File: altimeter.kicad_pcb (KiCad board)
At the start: 2 copper layers, 45 x 24 mm, 50 parts, among them J201 Conn_01x10, J202 Conn_ARM_JTAG_SWD_10, J203 Conn_02x03_Counter_Clockwise, J204 Conn_01x04, J205 USB_B_Micro, Q101 DMG2301L, Q302 BC847BDW1, Q402 BC847BDW1, Q502 BC847BDW1, U101 STM32F302CCTx, U102 MS5611-01BA, U103 MIC5219-3.3YM5, U104 LF50_TO252, U105 LM397, U106 MT25Q, U107 AIS2120SXTR, U301 SI7232DN, U501 SI7232DN, Y101 Crystal_Small

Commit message: more work on schematic and layout
Signed-off-by: Thomas Schmid <tom@lfence.de>
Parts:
- removed the R302 at (141.7, 98.0)
- removed R305, R405, R505: R, Resistor_SMD:R_0402_1005Metric
- removed the R402 at (128.3, 103.4)
- removed the R502 at (151.2, 130.5)
- added F301: Polyfuse, Fuse:Fuse_0603_1608Metric_Pad1.05x0.95mm_HandSolder, F.Cu at (142.0, 105.0)
- added F401: Polyfuse, Fuse:Fuse_0603_1608Metric_Pad1.05x0.95mm_HandSolder, F.Cu at (140.0, 115.5)
- added F501: Polyfuse, Fuse:Fuse_0603_1608Metric_Pad1.05x0.95mm_HandSolder, F.Cu at (140.5, 107.0)
- C101, C102: value C_Small -> 22p
- C104: renamed from C103; value C_Small -> 100n
- C107: renamed from C105; value C_Small -> 2.2u
- J203: footprint Connector_PinHeader_2.00mm:PinHeader_2x05_P2.00mm_Vertical_SMD -> Connector_PinHeader_2.54mm:PinHeader_2x03_P2.54mm_Horizontal
- R101, R102: value R -> 680
- R301, R401, R501: value R -> 2.7k
- R302: renamed from R303; value R -> 33
- R303: renamed from R304; value R -> 2.7k
- R402: renamed from R403; value R -> 33
- R403: renamed from R404; value R -> 2.7k
- R502: renamed from R503; value R -> 33
- R503: renamed from R504; value R -> 2.7k
- U101: moved to B.Cu
- U103: renamed from U107; moved to B.Cu
- U106: renamed from U105; moved to B.Cu
- U107: renamed from U102; moved to B.Cu
- moved D102 46.4 mm to (166.0, 99.0), turned to 90 degrees
- moved D101 45.1 mm to (164.5, 99.0), turned to 90 degrees
- moved J202 16.0 mm to (155.0, 117.0)
- moved U107 13.0 mm to (159.5, 106.5), turned to 90 degrees
- moved Q101 12.6 mm to (167.0, 106.0)
- moved U106 11.9 mm to (165.5, 104.0)
- moved Q401 11.7 mm to (140.5, 112.0)
- moved Y101 8.35 mm to (154.5, 124.5), turned to 180 degrees
- moved U102 6.36 mm to (169.0, 115.0)
- moved U103 5.93 mm to (172.5, 106.0), turned to 180 degrees
- moved U501 3.94 mm to (143.5, 115.5)
- moved U101 1.30 mm to (158.0, 115.5)
- turned U105 to 180 degrees
- renumbered C104 to C105, C107 to C106, C106 to C108, J205 to J204, J204 to J205, Q302 to Q301, Q402 to Q401, Q502 to Q501, U106 to U102, U103 to U104, U104 to U105

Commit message: update
Signed-off-by: Thomas Schmid <tom@lfence.de>
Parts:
- removed U106: LM397, Package_TO_SOT_SMD:SOT-23-5_HandSoldering
- removed Y101: Crystal_Small, Crystal:Crystal_SMD_5032-2Pin_5.0x3.2mm_HandSoldering
- added C103: 1u, Capacitor_SMD:C_0603_1608Metric_Pad1.05x0.95mm_HandSolder, B.Cu at (164.5, 107.4)
- added C3: CP, Capacitor_THT:CP_Axial_L11.0mm_D8.0mm_P15.00mm_Horizontal, F.Cu at (150.0, 100.4)
- added Y1: Crystal_GND24, Crystal:Crystal_SMD_2520-4Pin_2.5x2.0mm, B.Cu at (151.8, 118.2)
- C101, C102: footprint Capacitor_SMD:C_0603_1608Metric_Pad1.05x0.95mm_HandSolder -> Capacitor_SMD:C_0402_1005Metric; moved to B.Cu
- C104: footprint Capacitor_SMD:C_0603_1608Metric_Pad1.05x0.95mm_HandSolder -> Capacitor_SMD:C_0805_2012Metric_Pad1.15x1.40mm_HandSolder; moved to B.Cu
- C107, F301, F401, F501, Q101, Q301, Q401, Q501, R301, R302, R303, R401, R402, R403, R501, R502, R503, U301, U501: moved to B.Cu
- H201, H202: footprint MountingHole:MountingHole_3.2mm_M3_DIN965 -> MountingHole:MountingHole_3.2mm_M3_Pad_Via
- moved C107 47.8 mm to (153.2, 99.8)
- moved C104 44.1 mm to (153.4, 101.3)
- moved C106 41.5 mm to (157.4, 112.1)
- moved R102 39.3 mm to (168.0, 102.4), turned to 90 degrees
- moved R101 37.1 mm to (166.6, 102.4), turned to 90 degrees
- moved C101 37.1 mm to (154.0, 118.2), turned to 90 degrees
- moved R104 33.6 mm to (176.8, 104.0)
- moved R103 33.3 mm to (174.5, 104.3)
- moved C105 32.5 mm to (167.3, 108.1)
- moved Q501 29.9 mm to (141.4, 105.1)
- moved C108 29.8 mm to (172.8, 107.2)
- moved R503 29.5 mm to (139.0, 106.1)
- moved R502 28.5 mm to (139.4, 104.5), turned to 90 degrees
- moved R201 27.7 mm to (173.0, 102.9)
- moved C102 27.5 mm to (149.4, 118.2), turned to 270 degrees
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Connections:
- U301 pad 1: FIRE_PYRO1 -> FIRE_PYRO2
- U301 pad 3: FIRE_PYRO2 -> FIRE_PYRO1
- U301 pad 5: PYRO2_LOW -> PYRO1_LOW
- U301 pad 6: PYRO1_LOW -> PYRO2_LOW
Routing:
- net PYRO_TEST_ENABLE: track 0.00 -> 6.40 mm
- net Net-(Q501-Pad1): track 0.00 -> 4.28 mm
- net Net-(Q401-Pad1): track 0.00 -> 4.28 mm
- net GND: track 0.00 -> 4.22 mm
- net Net-(Q501-Pad2): track 0.00 -> 1.94 mm
- net Net-(Q401-Pad2): track 0.00 -> 1.94 mm
- net Net-(F501-Pad2): track 0.00 -> 1.48 mm
- net Net-(F401-Pad2): track 0.00 -> 1.48 mm
- net Net-(Q301-Pad2): track 3.29 -> 1.94 mm
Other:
- net class Default: clearance 0.2 -> 0.1651; trace_width 0.25 -> 0.1778
- rule trace_clearance: 0.2 -> 0.1651
- rule trace_min: 0.2 -> 0.1524

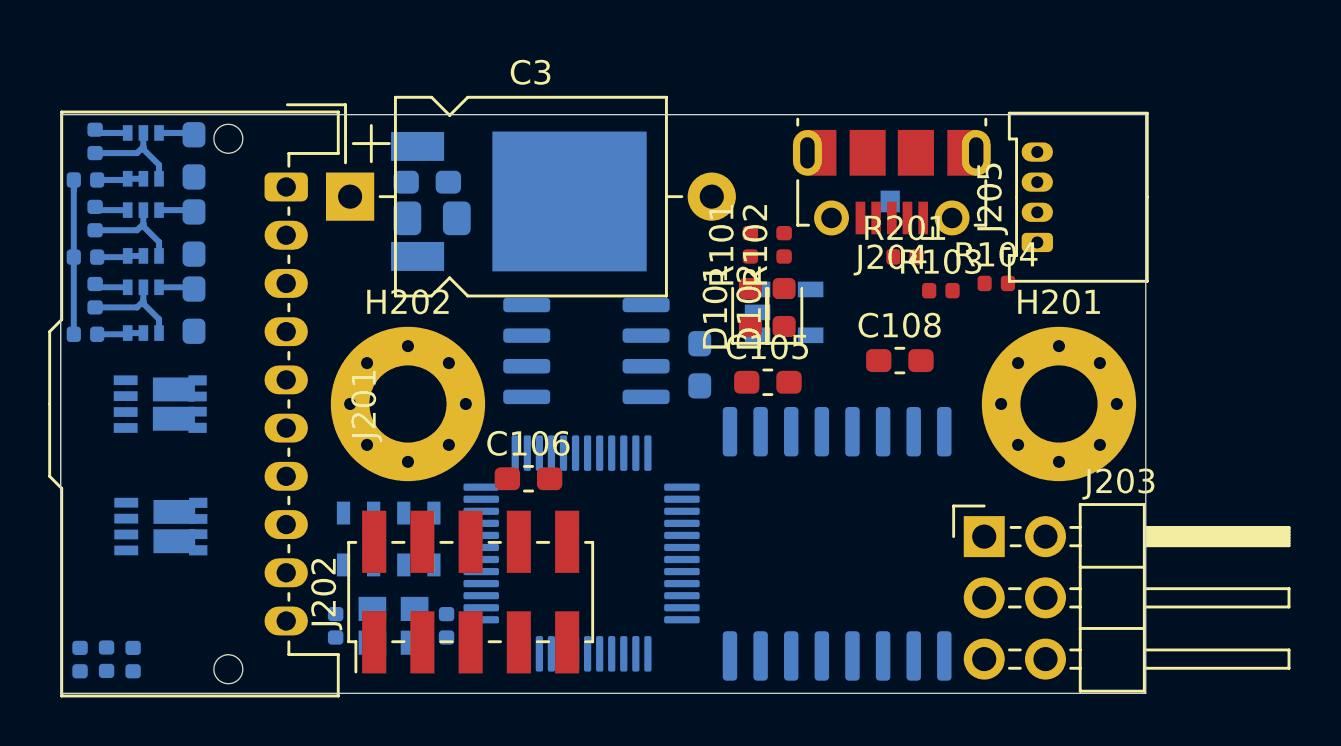
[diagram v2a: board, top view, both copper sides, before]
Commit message: update to schematic and layout
Signed-off-by: Thomas Schmid <tom@lfence.de>
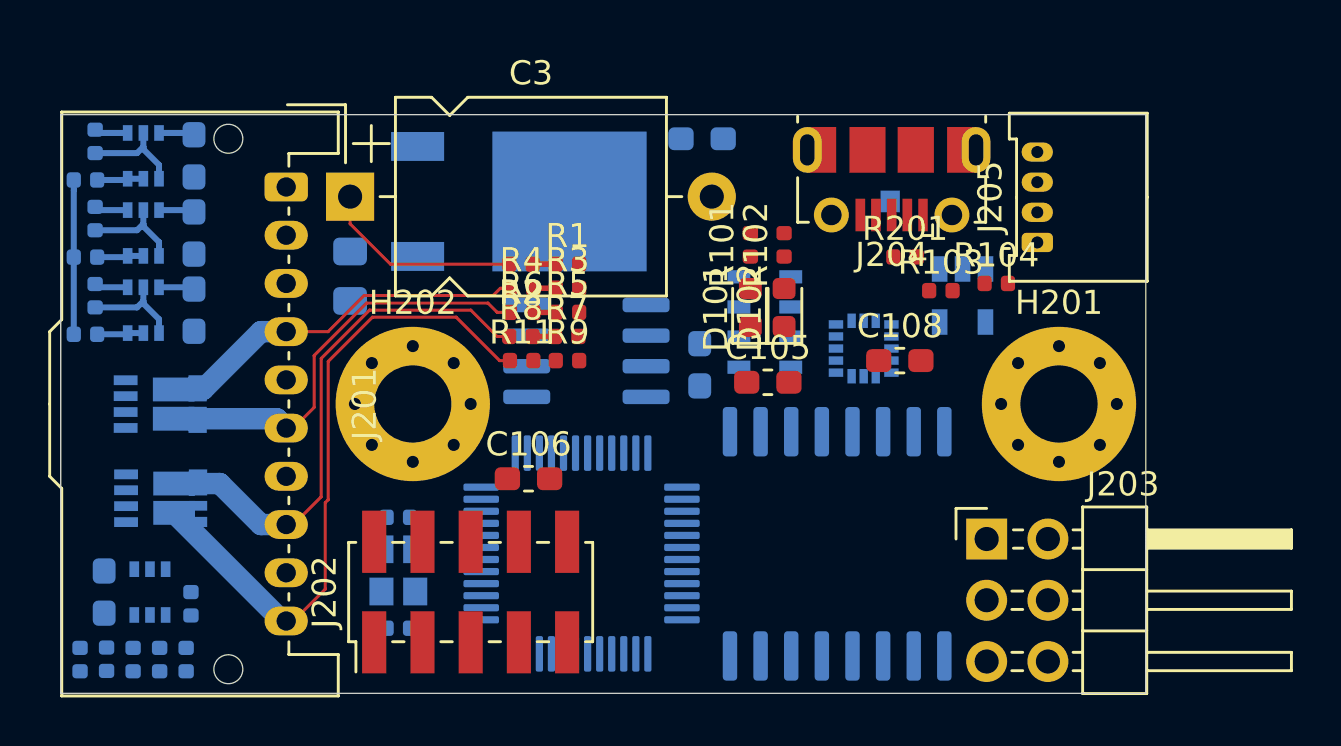
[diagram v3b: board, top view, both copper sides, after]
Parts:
- added F1: Polyfuse, Fuse:Fuse_0603_1608Metric_Pad1.05x0.95mm_HandSolder, B.Cu at (139.8, 116.8)
- added Q1: BC847BDW1, Package_TO_SOT_SMD:SOT-363_SC-70-6, B.Cu at (141.7, 116.8)
- added R1: 68k, Resistor_SMD:R_0402_1005Metric, F.Cu at (159.0, 103.2)
- added R10: 2.7k, Resistor_SMD:R_0402_1005Metric, B.Cu at (142.1, 119.6)
- added R11: 220k, Resistor_SMD:R_0402_1005Metric, F.Cu at (157.1, 107.2)
- added R12: 33, Resistor_SMD:R_0402_1005Metric, B.Cu at (143.4, 117.3)
- added R13: 2.7k, Resistor_SMD:R_0402_1005Metric, B.Cu at (143.2, 119.6)
- added R2: 220k, Resistor_SMD:R_0402_1005Metric, F.Cu at (157.1, 103.2)
- added R3: 68k, Resistor_SMD:R_0402_1005Metric, F.Cu at (159.0, 104.2)
- added R4: 220k, Resistor_SMD:R_0402_1005Metric, F.Cu at (157.1, 104.2)
- added R5: 68k, Resistor_SMD:R_0402_1005Metric, F.Cu at (159.0, 105.2)
- added R6: 220k, Resistor_SMD:R_0402_1005Metric, F.Cu at (157.1, 105.2)
- added R7: 68k, Resistor_SMD:R_0402_1005Metric, F.Cu at (159.0, 106.2)
- added R8: 220k, Resistor_SMD:R_0402_1005Metric, F.Cu at (157.1, 106.2)
- added R9: 68k, Resistor_SMD:R_0402_1005Metric, F.Cu at (159.0, 107.2)
- added U2: ICM-20602, Package_LGA:LGA-16_3x3mm_P0.5mm_LayoutBorder3x5y, B.Cu at (171.3, 106.7)
- C3: value CP -> 1m
- moved U107 18.0 mm to (167.2, 105.6), turned to 0 degrees
- moved C107 11.5 mm to (164.6, 98.0)
- moved U104 7.43 mm to (175.4, 104.5), turned to 270 degrees
- moved C101 4.92 mm to (152.0, 113.7), turned to 180 degrees
- moved C104 4.16 mm to (150.0, 103.7), turned to 270 degrees
- moved C102 2.60 mm to (152.0, 118.3), turned to 0 degrees
- moved Y1 2.31 mm to (152.0, 115.9), turned to 270 degrees
- moved U501 1.18 mm to (142.1, 112.9)
- moved H202 0.20 mm to (152.6, 109.0)
- moved J203 0.14 mm to (176.4, 114.6)
- moved J204 0.12 mm to (172.5, 99.7)
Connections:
- C104 pad 1: +BATT -> PYRO0_HIGH
- C3 pad 1: +BATT -> PYRO0_HIGH
- F301 pad 1: PYRO1_LOW -> PYRO0_LOW
- F401 pad 1: PYRO2_LOW -> PYRO1_LOW
- F501 pad 1: PYRO3_LOW -> PYRO2_LOW
- H201 pad 1: (no net) -> GND
- H202 pad 1: (no net) -> GND
- J201 pad 1: +BATT -> PYRO0_HIGH
- J201 pad 3: ARM_H -> PYRO0_HIGH
- J201 pad 4: ARM_L -> PYRO0_LOW
- J201 pad 5: ARM_LOW -> PYRO0_HIGH
- J201 pad 7: ARM_LOW -> PYRO0_HIGH
- J201 pad 9: ARM_LOW -> PYRO0_HIGH
- R103 pad 1: +BATT -> PYRO0_HIGH
- R301 pad 1: FIRE_PYRO1 -> FIRE_PYRO0
- R401 pad 1: FIRE_PYRO2 -> FIRE_PYRO1
- R501 pad 1: FIRE_PYRO3 -> FIRE_PYRO2
- U101 pad 10: PYRO1_LOW -> PYRO0_SENSE
- U101 pad 11: PYRO2_LOW -> PYRO1_SENSE
- U101 pad 12: PYRO3_LOW -> PYRO2_SENSE
- U101 pad 13: VBAT_SENSE -> PYRO3_SENSE
- U101 pad 14: Net-(U101-Pad14) -> VBAT_SENSE
- U101 pad 21: FIRE_PYRO2 -> FIRE_PYRO1
- U101 pad 22: FIRE_PYRO3 -> FIRE_PYRO2
- U101 pad 42: Net-(U101-Pad42) -> FIRE_PYRO3
- U101 pad 46: FIRE_PYRO1 -> FIRE_PYRO0
- U105 pad 1: +BATT -> PYRO0_HIGH
- U301 pad 1: FIRE_PYRO2 -> FIRE_PYRO1
- U301 pad 3: FIRE_PYRO1 -> FIRE_PYRO0
- U301 pad 5: PYRO1_LOW -> PYRO0_LOW
- U301 pad 6: PYRO2_LOW -> PYRO1_LOW
- U501 pad 3: (no net) -> FIRE_PYRO2
- U501 pad 4: (no net) -> GND
- U501 pad 5: (no net) -> PYRO2_LOW
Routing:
- net PYRO3_LOW: track 0.00 -> 27.2 mm
- net PYRO2_LOW: track 0.00 -> 22.1 mm
- net PYRO1_LOW: track 0.00 -> 17.7 mm
- net PYRO0_LOW: track 0.00 -> 15.7 mm
- net PYRO0_HIGH: track 0.00 -> 8.42 mm
- net VBAT_SENSE: track 0.00 -> 0.96 mm
- net PYRO2_SENSE: track 0.00 -> 0.93 mm
- net PYRO1_SENSE: track 0.00 -> 0.93 mm
- net PYRO0_SENSE: track 0.00 -> 0.93 mm
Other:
- rule pad_to_mask_clearance: 0.051 -> 0.0254
- rule solder_mask_min_width: 0.25 -> 0.127
- rule trace_min: 0.1524 -> 0.127
- rule via_min_drill: 0.3 -> 0.2
- rule via_min_size: 0.4 -> 0.45

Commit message: more work on schematic and layout
Signed-off-by: Thomas Schmid <tom@binary-kitchen.de>
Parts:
- added D103: 1N4148WS, Diode_SMD:D_SOD-323, F.Cu at (169.6, 109.8)
- added LS101: Speaker_Crystal, altimeter:CSS-95B30-SMT, F.Cu at (167.7, 115.6)
- added Q102: DMG2301L, Package_TO_SOT_SMD:SOT-23, F.Cu at (173.3, 108.4)
- moved C103 6.78 mm to (167.5, 101.3)
- moved C102 4.50 mm to (152.0, 113.8), turned to 180 degrees
- moved C101 4.30 mm to (152.0, 118.0), turned to 0 degrees
- moved R201 3.11 mm to (169.9, 102.9), turned to 180 degrees
- moved C108 2.58 mm to (174.7, 105.4)
- moved R13 1.04 mm to (143.7, 118.7), turned to 180 degrees
- moved R12 0.90 mm to (144.3, 117.2)
- moved Q1 0.67 mm to (142.3, 116.5)
- moved F1 0.67 mm to (140.4, 116.5)
- moved R10 0.30 mm to (142.1, 119.9)
- moved R301 0.30 mm to (138.8, 119.9)
- moved R401 0.30 mm to (139.9, 119.9)
- moved R501 0.30 mm to (141.0, 119.9)
- turned U107 to 180 degrees
- turned Y1 to 90 degrees
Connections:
- net Net-(U101-Pad30) renamed UART1_TX
- net Net-(U101-Pad31) renamed UART1_RX
- net USB_DM renamed USB_D_N
- net USB_DP renamed USB_D_P
- U101 pad 19: Net-(U101-Pad19) -> SUMMER
- U101 pad 20: Net-(U101-Pad20) -> BARO_CSS
- U101 pad 21: FIRE_PYRO1 -> ACC_CS
- U101 pad 22: FIRE_PYRO2 -> IMU_CS
- U101 pad 40: Net-(U101-Pad40) -> FIRE_PYRO0
- U101 pad 41: Net-(U101-Pad41) -> FIRE_PYRO1
- U101 pad 42: FIRE_PYRO3 -> FIRE_PYRO2
- U101 pad 43: BARO_CSS -> FIRE_PYRO3
- U101 pad 45: ACC_CS -> PWM1
- U101 pad 46: FIRE_PYRO0 -> PWM2
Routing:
- net USB_D_P: track 0.00 -> 24.1 mm, vias 0 -> 1
- net USB_D_N: track 0.00 -> 24.0 mm, vias 0 -> 1
- net FIRE_PYRO0: track 0.00 -> 13.1 mm
- net FIRE_PYRO1: track 0.00 -> 11.7 mm
- net FIRE_PYRO2: track 0.00 -> 9.53 mm
- net FIRE_PYRO3: track 0.00 -> 8.59 mm
- net Net-(F1-Pad2): track 0.00 -> 5.03 mm
- net Net-(C101-Pad1): track 0.00 -> 4.91 mm
- net SPI1_MISO: track 0.00 -> 4.35 mm
- net SPI1_MOSI: track 0.00 -> 4.34 mm
- net SPI1_SCK: track 0.00 -> 4.33 mm
- net Net-(Q1-Pad1): track 0.00 -> 3.62 mm
- net PYRO3_LOW: track 27.2 -> 30.8 mm
- net Net-(C102-Pad1): track 0.00 -> 3.37 mm
- net Net-(Q1-Pad2): track 0.00 -> 1.73 mm

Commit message: major work on layout. nearly finished
Signed-off-by: Thomas Schmid <tom@binary-kitchen.de>
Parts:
- removed D102: LED, LED_SMD:LED_0603_1608Metric
- removed R102: 680, Resistor_SMD:R_0402_1005Metric
- removed U2: ICM-20602, Package_LGA:LGA-16_3x3mm_P0.5mm_LayoutBorder3x5y
- added C1: 100n, Capacitor_SMD:C_0402_1005Metric, F.Cu at (174.5, 116.9)
- added C109: 100n, Capacitor_SMD:C_0402_1005Metric, B.Cu at (174.5, 108.2)
- added C110: 100n, Capacitor_SMD:C_0402_1005Metric, B.Cu at (174.6, 107.1)
- added C111: C_Small, Capacitor_SMD:C_0402_1005Metric, B.Cu at (163.3, 111.0)
- added C112: C_Small, Capacitor_SMD:C_0402_1005Metric, B.Cu at (153.1, 114.2)
- added C113: C_Small, Capacitor_SMD:C_0402_1005Metric, B.Cu at (155.3, 119.4)
- added C114: C_Small, Capacitor_SMD:C_0402_1005Metric, B.Cu at (154.0, 114.2)
- added C115: C_Small, Capacitor_SMD:C_0402_1005Metric, B.Cu at (163.8, 118.9)
- added C116: C_Small, Capacitor_SMD:C_0402_1005Metric, B.Cu at (163.8, 119.7)
- added C2: 100n, Capacitor_SMD:C_0402_1005Metric, B.Cu at (155.5, 104.9)
- added U1: LMV331, Package_TO_SOT_SMD:SOT-23-5, F.Cu at (170.0, 105.5)
- C105, C108: moved to B.Cu
- C106: footprint Capacitor_SMD:C_0603_1608Metric_Pad1.05x0.95mm_HandSolder -> Capacitor_SMD:C_0402_1005Metric; moved to B.Cu
- U102: value MT25Q -> S25L512S
- moved C103 14.9 mm to (153.0, 104.5), turned to 0 degrees
- moved C106 13.2 mm to (168.3, 104.6), turned to 90 degrees
- moved R101 11.7 mm to (158.9, 111.3), turned to 270 degrees
- moved D101 11.0 mm to (157.8, 111.6)
- moved C105 10.5 mm to (177.2, 104.3), turned to 90 degrees
- moved R104 9.14 mm to (167.8, 105.6), turned to 270 degrees
- moved R103 6.73 mm to (167.8, 103.6), turned to 270 degrees
- moved Q102 4.09 mm to (175.6, 105.1)
- moved D103 3.86 mm to (173.4, 109.7), turned to 180 degrees
- moved C108 2.20 mm to (172.7, 104.4), turned to 90 degrees
- moved R1 1.52 mm to (160.3, 104.0)
- moved R3 1.50 mm to (160.3, 104.9)
- moved R5 1.48 mm to (160.3, 105.9)
- moved R7 1.46 mm to (160.3, 106.8)
- moved R9 1.44 mm to (160.3, 107.8)
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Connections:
- net BARO_CSS renamed IMU_GYRO_CS
- net JTCK renamed SWCLK
- net JTDO renamed SWO
- net JTMS renamed SWDIO
- J202 pad 8: JTDI -> Net-(J202-Pad8)
- U101 pad 18: Net-(U101-Pad18) -> ACC_CS
- U101 pad 19: SUMMER -> BARO_CS
- U101 pad 21: ACC_CS -> IMU_ACC_CS
- U101 pad 22: IMU_CS -> SUMMER
- U101 pad 38: JTDI -> INT1
- U101 pad 6: LED2 -> INT2
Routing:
- net GND: track 4.22 -> 99.7 mm, vias 0 -> 47
- net PYRO_TEST_ENABLE: track 6.40 -> 52.8 mm, vias 0 -> 3
- net +5V: track 0.00 -> 45.6 mm, vias 0 -> 13
- net +3V3: track 0.00 -> 40.0 mm, vias 0 -> 9
- net FIRE_PYRO0: track 13.1 -> 45.2 mm, vias 0 -> 5
- net FIRE_PYRO1: track 11.7 -> 40.4 mm, vias 0 -> 5
- net FIRE_PYRO2: track 9.53 -> 33.2 mm, vias 0 -> 3
- net FIRE_PYRO3: track 8.59 -> 28.4 mm, vias 0 -> 3
- net SUMMER: track 0.00 -> 18.1 mm, vias 0 -> 1
- net PYRO0_HIGH: track 8.42 -> 25.5 mm
- net Net-(D103-Pad2): track 0.00 -> 15.7 mm
- net SWDIO: track 0.00 -> 14.7 mm, vias 0 -> 1
- net Net-(Q101-Pad2): track 0.00 -> 13.8 mm, vias 0 -> 1
- net SPI2_MISO: track 0.00 -> 13.3 mm, vias 0 -> 2
- net PYRO0_SENSE: track 0.93 -> 13.5 mm, vias 0 -> 3
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- added copper zone on In2.Cu, net +3V3
- added copper zone on In2.Cu, net +5V
- added copper zone on B.Cu, net GND
- added copper zone on F.Cu, net GND
- added copper zone on In1.Cu, net GND
- added copper zone on In2.Cu, net GND
- added copper zone on F.Cu, net PYRO0_HIGH
- added copper zone on In1.Cu, net PYRO0_HIGH
- added copper zone on B.Cu, net PYRO0_LOW
- added copper zone on In2.Cu, net PYRO0_LOW
- added copper zone on B.Cu, net PYRO1_LOW
- added copper zone on In2.Cu, net PYRO1_LOW
- added copper zone on B.Cu, net PYRO2_LOW
- added copper zone on In2.Cu, net PYRO2_LOW
- added copper zone on B.Cu, net PYRO3_LOW
- added copper zone on In2.Cu, net PYRO3_LOW
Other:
- copper layers 2 -> 4
- board text added: "JLCJLCJLCJLC"
